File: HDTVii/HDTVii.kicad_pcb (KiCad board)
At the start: 2 copper layers, 18 parts

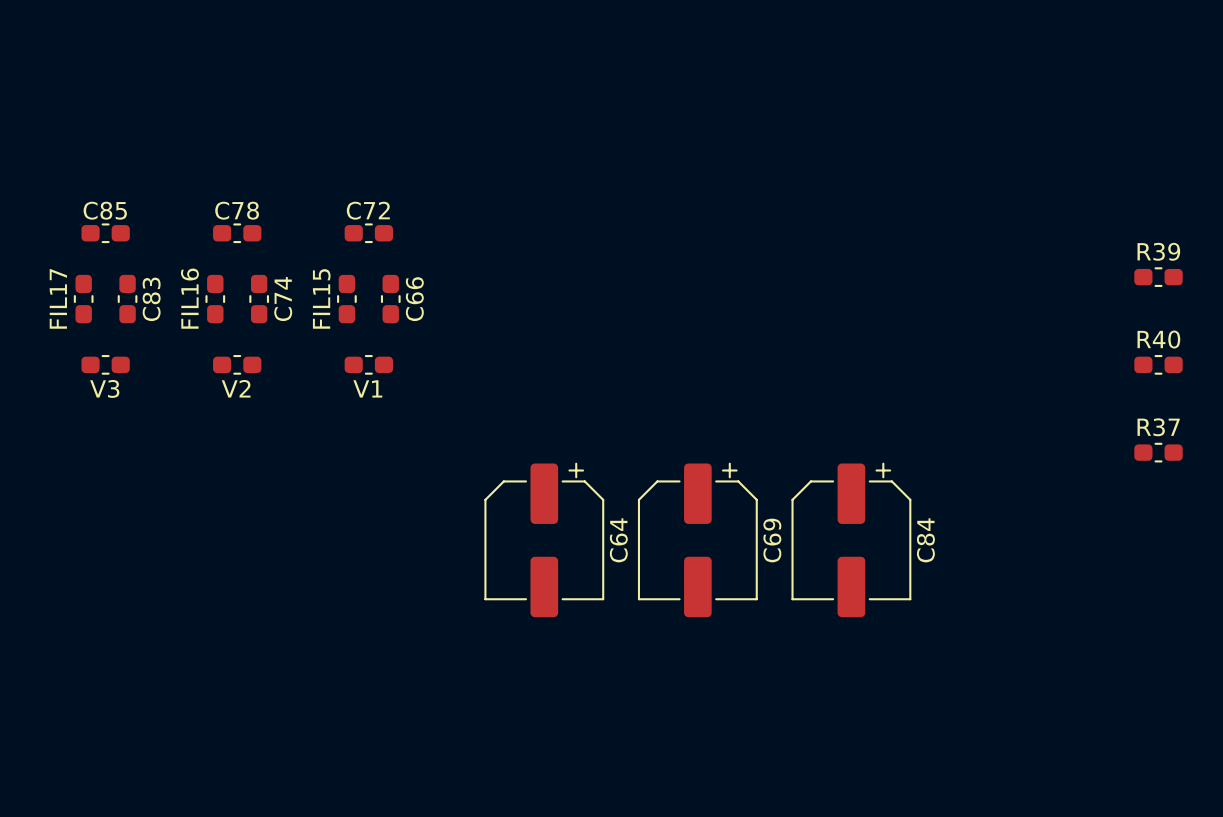
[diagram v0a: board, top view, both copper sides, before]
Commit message: Created PCB design and added footprint refs to parts.
Also changed stuff in the Schematic
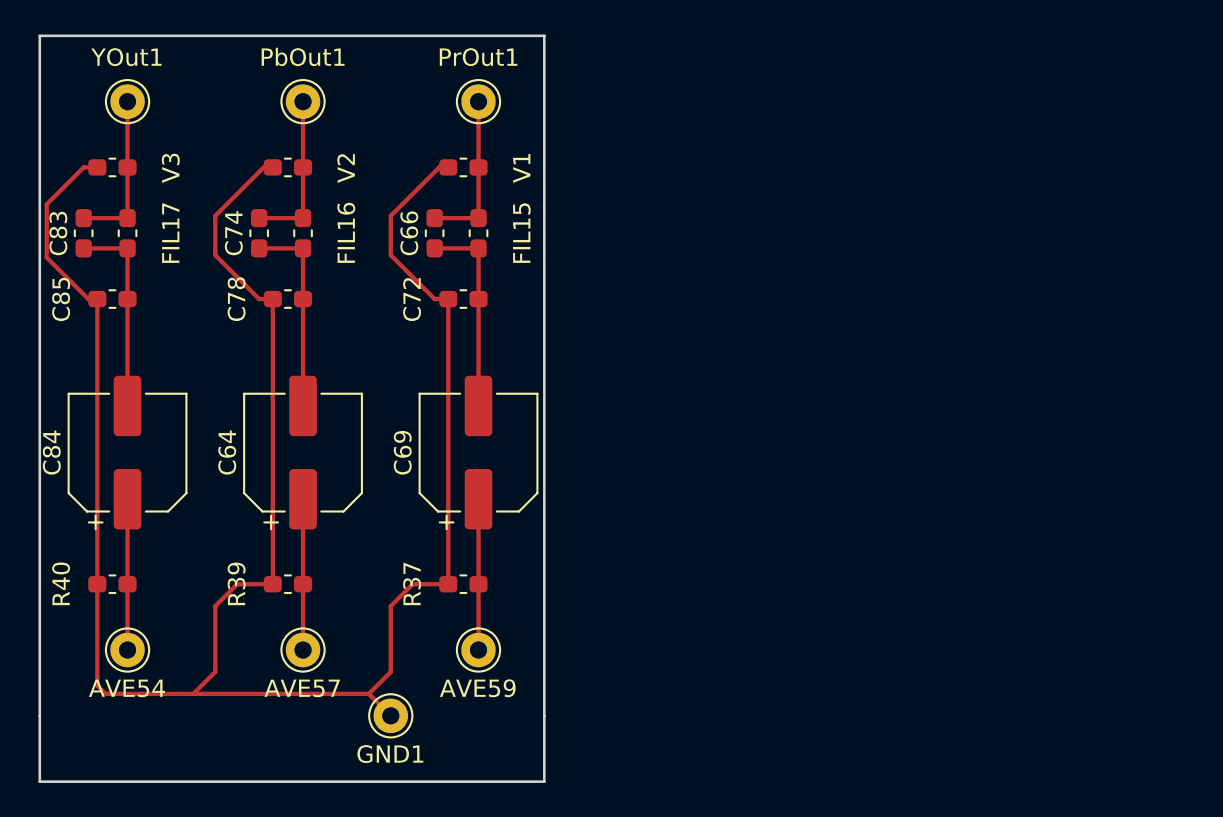
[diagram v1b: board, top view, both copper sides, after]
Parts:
- added AVE54: TestPoint, Connector_Pin:Pin_D1.0mm_L10.0mm, F.Cu at (102.9, 106.7)
- added AVE57: TestPoint, Connector_Pin:Pin_D1.0mm_L10.0mm, F.Cu at (113.0, 106.7)
- added AVE59: TestPoint, Connector_Pin:Pin_D1.0mm_L10.0mm, F.Cu at (123.2, 106.7)
- added GND1: TestPoint, Connector_Pin:Pin_D1.0mm_L10.0mm, F.Cu at (118.1, 110.5)
- added PbOut1: TestPoint, Connector_Pin:Pin_D1.0mm_L10.0mm, F.Cu at (113.0, 74.9)
- added PrOut1: TestPoint, Connector_Pin:Pin_D1.0mm_L10.0mm, F.Cu at (123.2, 74.9)
- added YOut1: TestPoint, Connector_Pin:Pin_D1.0mm_L10.0mm, F.Cu at (102.9, 74.9)
- FIL15, FIL16, FIL17: value ?H -> 390nH
- moved R40 61.9 mm to (102.0, 102.9), turned to 180 degrees
- moved R39 53.4 mm to (112.2, 102.9), turned to 180 degrees
- moved C84 42.2 mm to (102.9, 95.2), turned to 90 degrees
- moved R37 41.0 mm to (122.3, 102.9)
- moved C64 14.9 mm to (113.0, 95.2), turned to 90 degrees
- moved C69 13.7 mm to (123.2, 95.2), turned to 90 degrees
- moved V1 12.7 mm to (122.3, 78.7), turned to 0 degrees
- moved V2 11.8 mm to (112.2, 78.7), turned to 0 degrees
- moved V3 11.4 mm to (102.0, 78.7), turned to 0 degrees
- moved FIL15 8.52 mm to (123.2, 82.5), turned to 270 degrees
- moved C72 6.67 mm to (122.3, 86.4), turned to 0 degrees
- moved FIL16 6.35 mm to (113.0, 82.5), turned to 270 degrees
- moved C78 4.81 mm to (112.2, 86.4), turned to 0 degrees
- moved C66 4.58 mm to (120.7, 82.5), turned to 90 degrees
- moved C83 4.58 mm to (100.3, 82.5), turned to 90 degrees
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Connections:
- net AVE54 renamed Net-(AVE54-Pad1)
- net AVE57 renamed Net-(AVE57-Pad1)
- net AVE59 renamed Net-(AVE59-Pad1)
- net PbOut renamed Net-(C74-Pad2)
- net PrOut renamed Net-(C66-Pad2)
- net YOut renamed Net-(C83-Pad2)
- C69 pad 2: Net-(C69-Pad2) -> Net-(C66-Pad1)
- C72 pad 1: Net-(C72-Pad1) -> GND
- C74 pad 1: Net-(C74-Pad1) -> Net-(C64-Pad2)
- C78 pad 1: Net-(C78-Pad1) -> GND
- C78 pad 2: Net-(C74-Pad1) -> Net-(C64-Pad2)
- C84 pad 2: Net-(C84-Pad2) -> Net-(C83-Pad1)
- C85 pad 1: Net-(C85-Pad1) -> GND
- FIL16 pad 2: Net-(C74-Pad1) -> Net-(C64-Pad2)
- R37 pad 1: Net-(R37-Pad1) -> GND
- R39 pad 2: Net-(R39-Pad2) -> GND
- R40 pad 2: Net-(R40-Pad2) -> GND
- V1 pad 1: Net-(V1-Pad1) -> GND
- V2 pad 1: Net-(V2-Pad1) -> GND
- V3 pad 1: Net-(V3-Pad1) -> GND
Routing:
- net GND: track 0.00 -> 125.2 mm
- net Net-(C83-Pad1): track 0.00 -> 11.7 mm
- net Net-(C64-Pad2): track 0.00 -> 11.7 mm
- net Net-(C66-Pad1): track 0.00 -> 11.7 mm
- net Net-(C83-Pad2): track 0.00 -> 9.28 mm
- net Net-(C74-Pad2): track 0.00 -> 9.28 mm
- net Net-(C66-Pad2): track 0.00 -> 9.28 mm
- net Net-(AVE59-Pad1): track 0.00 -> 8.73 mm
- net Net-(AVE57-Pad1): track 0.00 -> 8.73 mm
- net Net-(AVE54-Pad1): track 0.00 -> 8.73 mm
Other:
- board outline added: 29.2 x 43.2 mm
